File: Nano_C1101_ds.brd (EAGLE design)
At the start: 46.7 x 29.2 mm, 9 parts

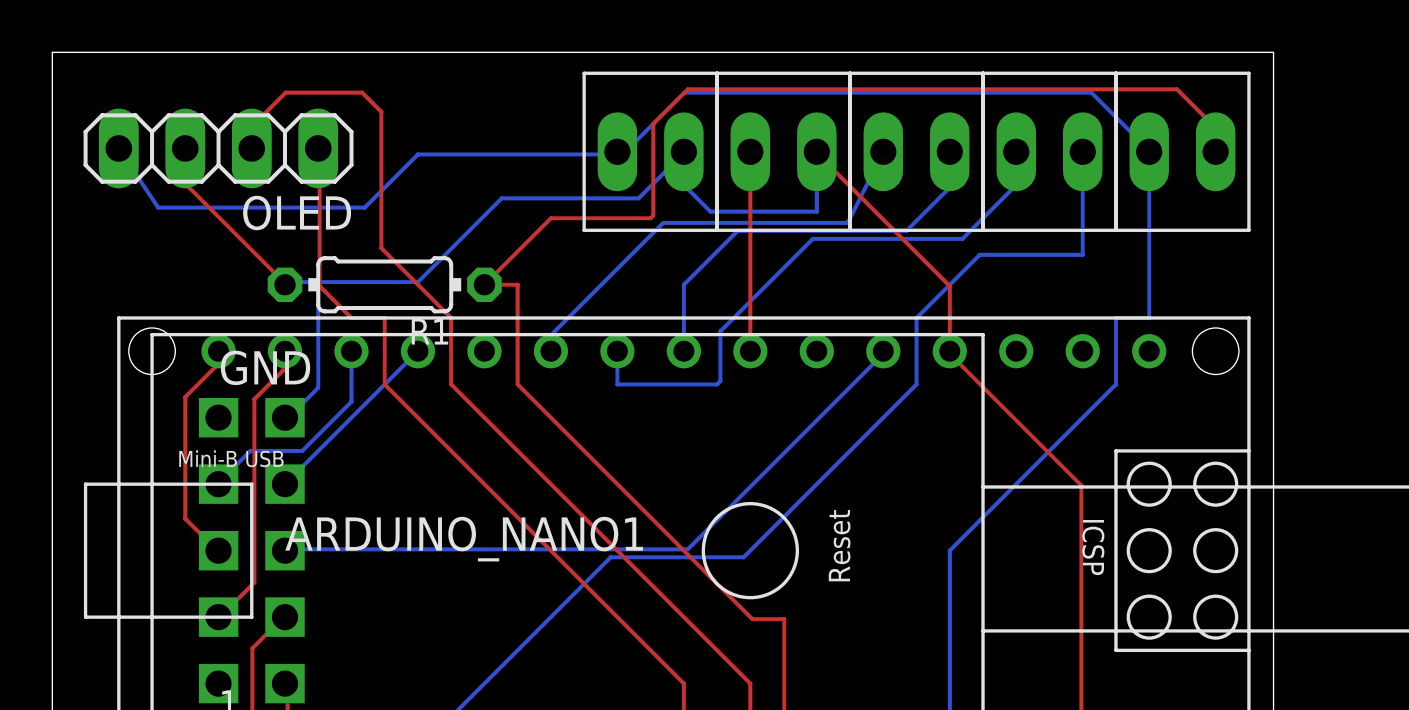
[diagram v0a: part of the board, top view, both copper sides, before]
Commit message: Added text on PCB
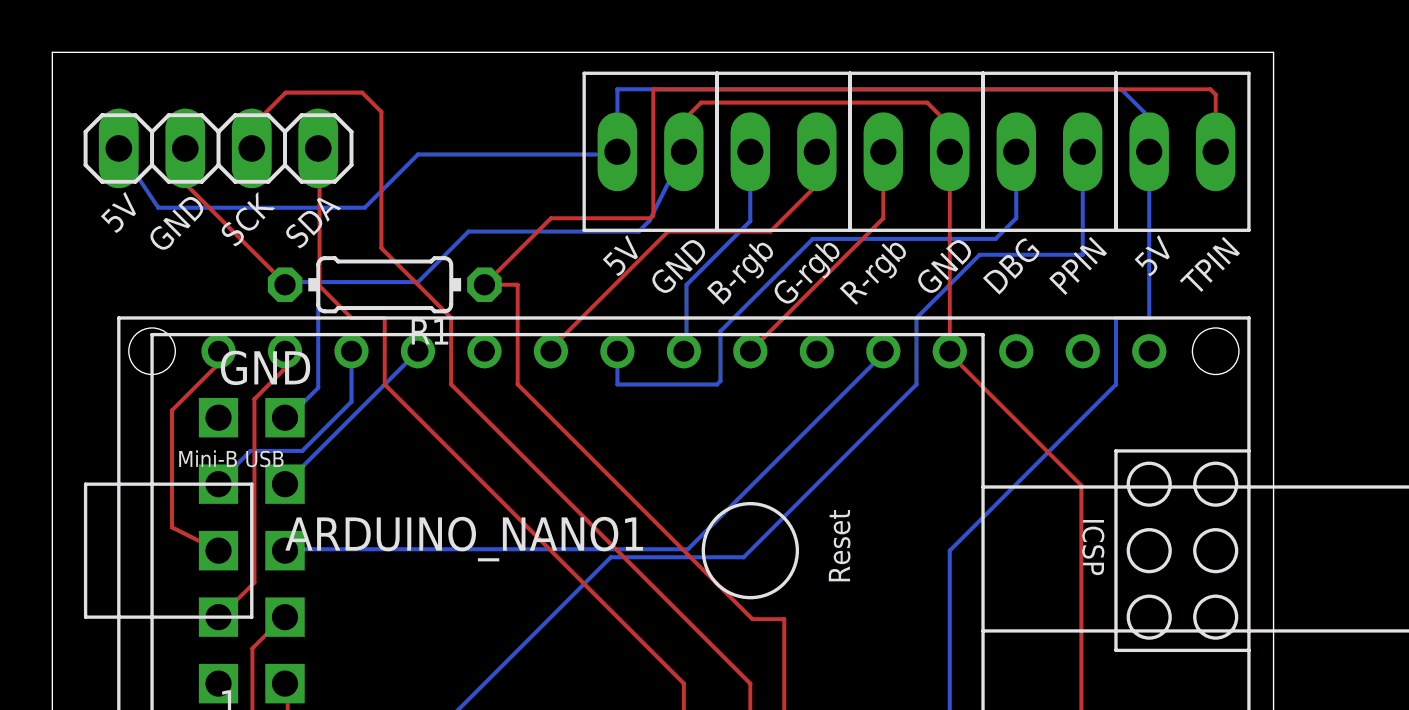
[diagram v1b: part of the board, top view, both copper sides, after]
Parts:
- moved G--B 5.08 mm to (27.9, 25.4), turned to 180 degrees
- moved R--GND 5.08 mm to (33.0, 25.4)
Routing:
- net B-RGB: track 15.6 -> 8.69 mm
- net G-RGB: track 16.8 -> 14.1 mm
- net GND: track 66.0 -> 68.4 mm
- net 5V: track 70.1 -> 72.4 mm
- net R-RGB: track 7.62 -> 9.72 mm
- net TPIN: track 69.5 -> 71.1 mm
- net MISO: track 8.69 -> 9.46 mm
- net DEBUG: track 22.1 -> 22.8 mm
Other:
- board text added: "5V"
- board text added: "B-rgb"
- board text added: "DBG"
- board text added: "G-rgb"
- board text added: "GND"
- board text added: "PPIN"
- board text added: "R-rgb"
- board text added: "SCK"
- board text added: "SDA"
- board text added: "TPIN"
